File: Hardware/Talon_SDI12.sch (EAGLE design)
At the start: 100 parts, among them J1 CONN_APOGEE_LOGGER, J2 CONN_TALON_REMOTE, J3 CONN_SDI-12_LOGGERM8_TE_BOARD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, J4 CONN_SDI-12_LOGGERM8_TE_BOARD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, J5 CONN_SDI-12_LOGGERM8_TE_BOARD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, Q1 2N7002, Q2 2N7002, Q3 2N7002, Q4 2N7002, Q5 AO3419, Q6 AO3419, Q7 AO3419, Q8 AO3419, U1 SN74HC04, U10 FXMAR2102UMLP, U11 74HC4852, U12 SN74AUP1T157DCK, U13 MCP3221, U14 MCP23018QFN, U15 PCA9536DFN, U16 MCP3421A3, U17 SN74LVC1G3157SC70, U18 SN74LVC1G3157SC70, U19 SN74LVC1G3157SC70, U2 CD4044, U20 SN74LVC1G3157SC70, U21 SN74LVC1G00SC70, U22 SN74LVC2G241DCU, U23 SN74LVC1G17DCK, U24 24AA02SOT23, U3 SIP32431TDFN, U4 INA4180A2, U5 MAX9034TSSOP, U6 SI1869, U7 SN74AC08, U8 LM2621, U9 LMR62014SOT23

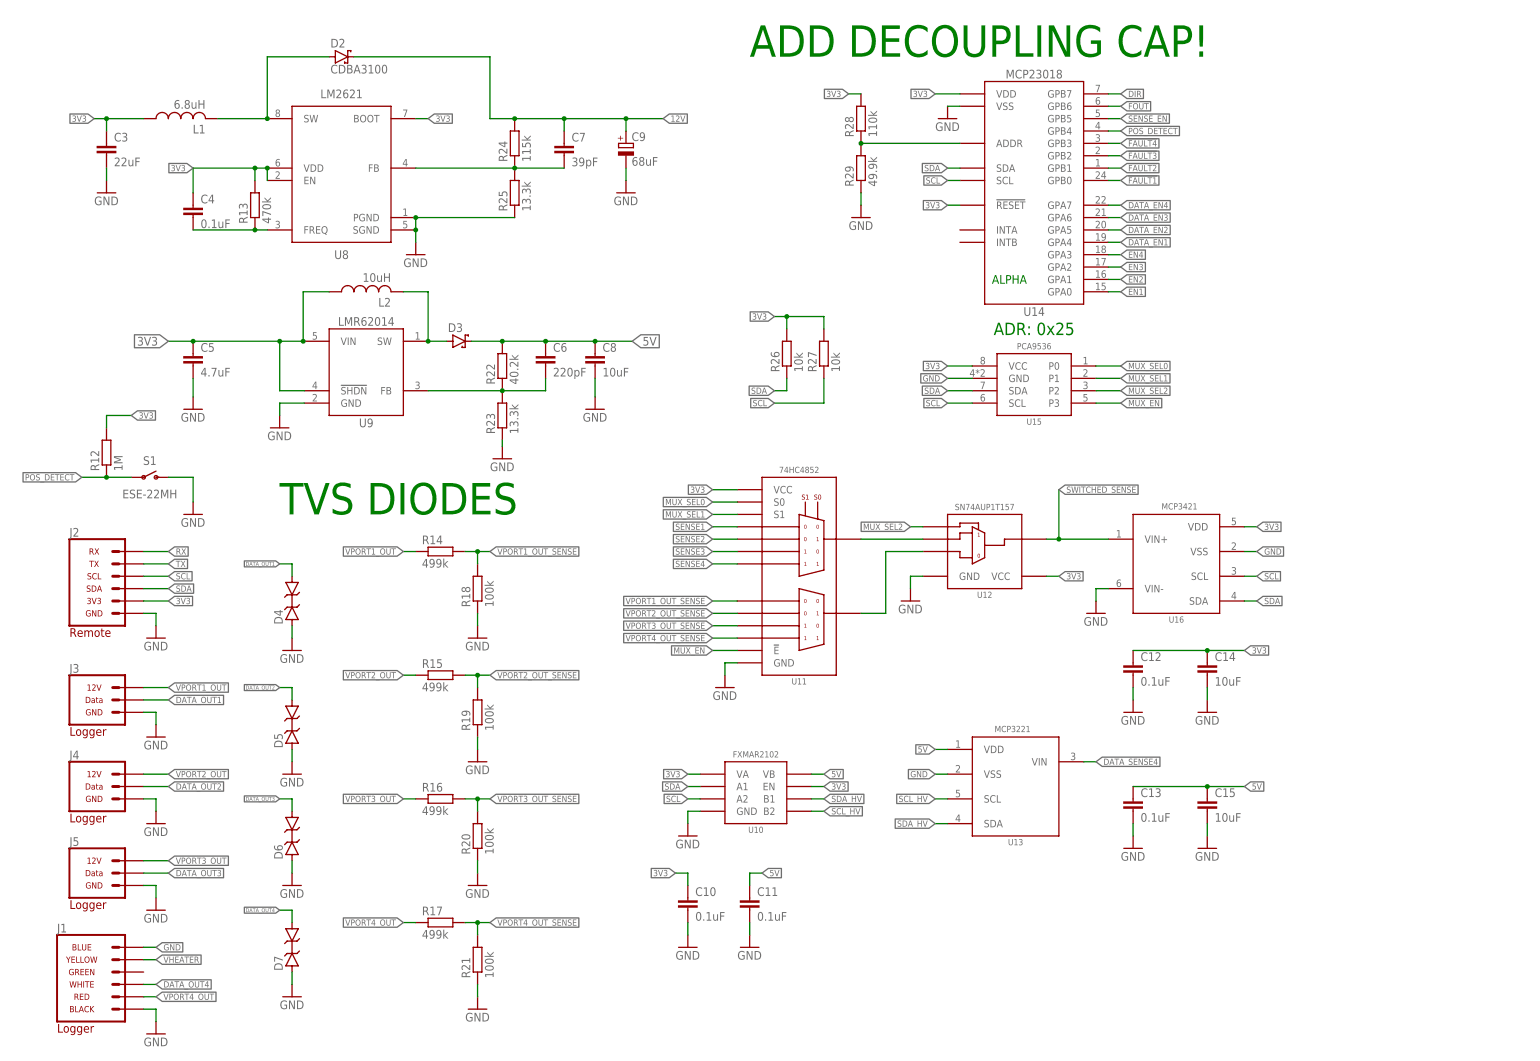
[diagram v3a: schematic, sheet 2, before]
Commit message: Updated v1.0, sent to fab
Made fixes for v1.0:
- Fixed bypass control
- Changed arrangement of 12V reg
- Added filter lines (clitch protection) to sense lines
- Flipped Talon connector port pinout
- Adjusted port 4 topology to deal with pulldown issue
- Moved MUX (U11/U15) to prevent soldering issues 
- Moved U7 to prevent bumping 
- Added additional protection circuitry on SDI-12 outputs
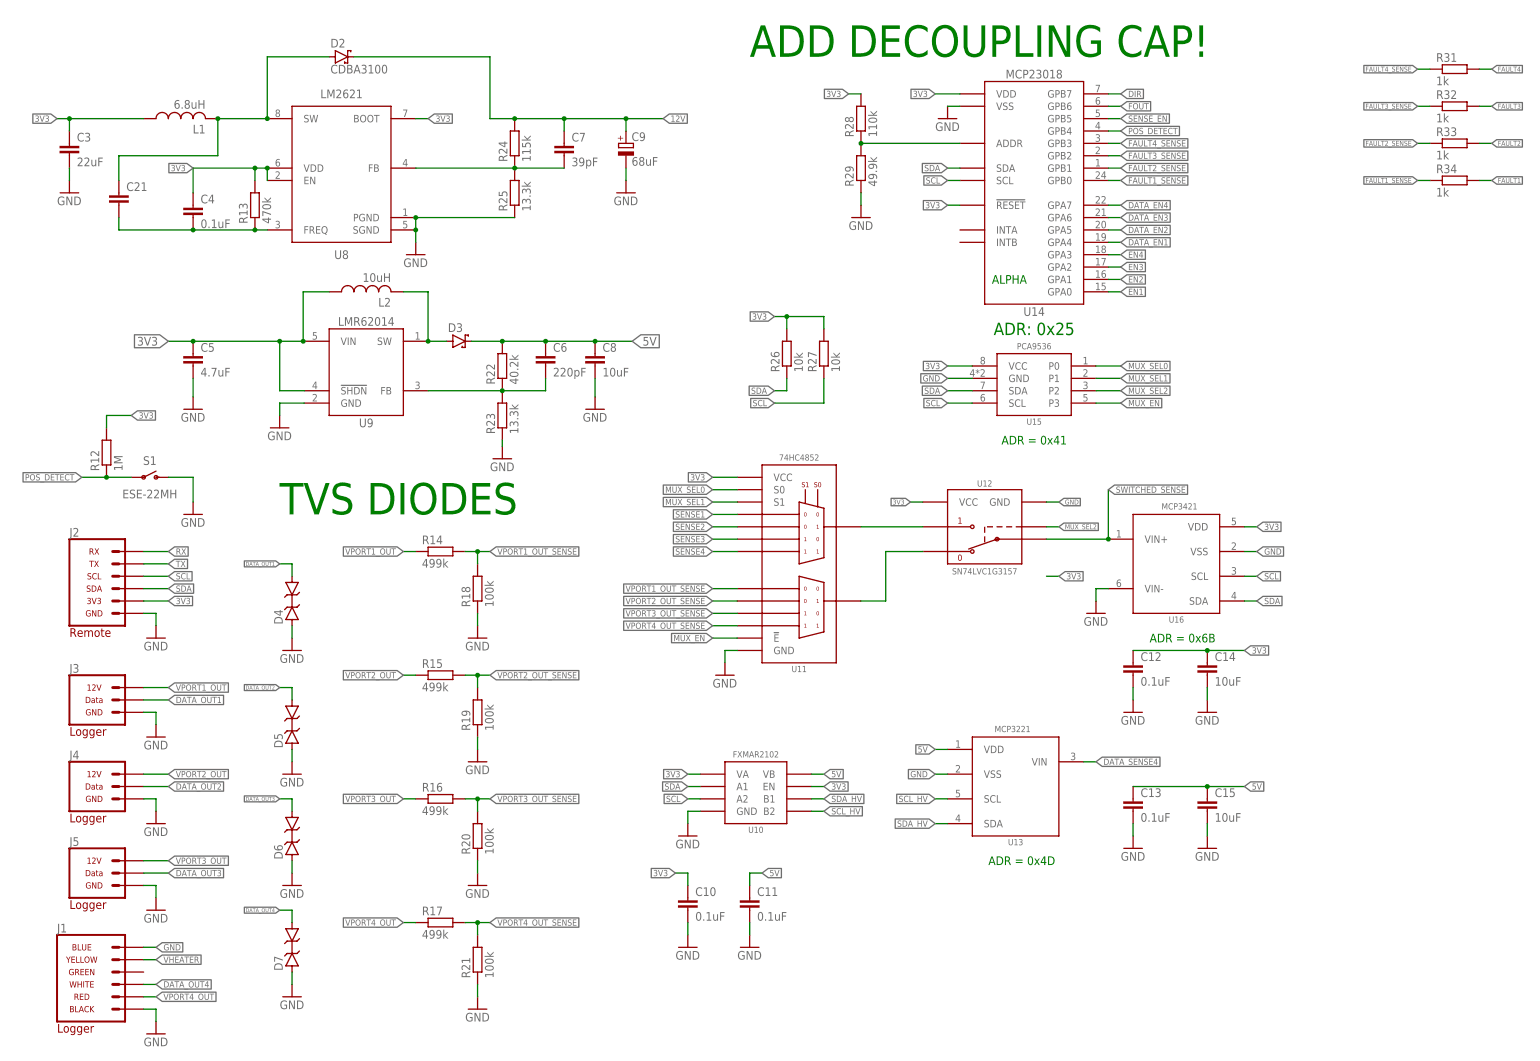
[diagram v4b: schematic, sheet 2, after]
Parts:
- removed R30: 100k, bschulz_passives:R-EU_100KR0402
- added C17, C18, C19, C20: 0.1uF, bschulz_passives:C-EU0.1UFC0402
- added C21: (no value), bschulz_passives:C-EUC0402
- added C22: 3.3nF, bschulz_passives:C-EUC0402
- added D10, D11, D8, D9: (no value), bschulz:DIODE_ZENERSOD-323
- added R31, R32, R33, R34, R35, R36, R37, R38: 1k, bschulz_passives:R-EU_1KR0402
- added R39: 200K, bschulz_passives:R-EU_200KR0402
- added R40, R41, R42, R43, R44: 510R, bschulz_passives:R-EU_R0402
- U12: value SN74AUP1T157DCK -> SN74LVC1G3157SC70; device bschulz:SN74AUP1T157DCK -> bschulz:SN74LVC1G3157SC70
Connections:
- new net !DATA_EN4: U1.Y5, U20.S, U6.EN
- new net DATA_OUT_PROTEC1: D8.C, R40.2, U17.A
- new net DATA_OUT_PROTEC2: D9.C, R42.2, U18.A
- new net DATA_OUT_PROTEC3: D10.C, R43.2, U19.A
- new net DATA_OUT_PROTEC4: D11.C, R44.2, U20.A
- new net DATA_PROTEC: R41.2, U22.1A, U22.2Y
- new net FAULT1_SENSE: R34.1, U14.GPB0
- new net FAULT2_SENSE: R33.1, U14.GPB1
- new net FAULT3_SENSE: R32.1, U14.GPB2
- new net FAULT4_SENSE: R31.1, U14.GPB3
- new net SENSE1_FILT: C17.1, R35.2, U5.INA-
- new net SENSE2_FILT: C18.1, R36.2, U5.INB-
- new net SENSE3_FILT: C19.1, R37.2, U5.INC-
- new net SENSE4_FILT: C20.1, R38.2, U5.IND-
- net !FAULT1: now also U1.Y4, U7.B4; no longer U1.A4, U14.GPB0, U2.Q2
- net !FAULT2: now also U1.Y2, U7.B1; no longer U1.A2, U14.GPB1, U2.Q1
- net !FAULT3: now also U1.Y3, U7.B3; no longer U1.A3, U14.GPB2, U2.Q3
- net !FAULT4: now also U1.Y1, U7.B2; no longer U1.A1, U14.GPB3, U2.Q4
- net 3V3: no longer U1.A5, U2.EN
- net DATA: now also C22.1, R39.2, R41.1, U20.B1; no longer U20.B2, U22.1A, U22.2Y
- net DATA_EN4: now also U1.A5; no longer R30.2, U20.S, U6.EN
- net DATA_OUT1: now also R40.1; no longer U17.A
- net DATA_OUT2: now also R42.1; no longer U18.A
- net DATA_OUT3: now also R43.1; no longer U19.A
- net DATA_OUT4: now also R44.1; no longer U20.A
- net DATA_SENSE4: now also U20.B2; no longer U20.B1
- net FAULT1: now also R34.2, U1.A4, U2.Q2; no longer U1.Y4, U7.B4
- net FAULT2: now also R33.2, U1.A2, U2.Q1; no longer U1.Y2, U7.B1
- net FAULT3: now also R32.2, U1.A3, U2.Q3; no longer U1.Y3, U7.B3
- net FAULT4: now also R31.2, U1.A1, U2.Q4; no longer U1.Y1, U7.B2
- net GND: now also C17.2, C18.2, C19.2, C20.2, C22.2, D10.A, D11.A, D8.A, D9.A, R39.1; no longer R30.1
- net MUX_SEL2: now also U12.S; no longer U12.C
- net N$18: now also U12.B1; no longer U12.B
- net N$38: now also U12.B2; no longer U12.A
- net N$7: now also C21.2
- net N$8: now also C21.1
- net SENSE1: now also R35.1; no longer U5.INA-
- net SENSE2: now also R36.1; no longer U5.INB-
- net SENSE3: now also R37.1; no longer U5.INC-
- net SENSE4: now also R38.1; no longer U5.IND-
- net SENSE_EN: now also U2.EN
- net SWITCHED_SENSE: now also U12.A; no longer U12.Y
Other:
- note added: "ADR = 0x41"
- note added: "ADR = 0x4D"
- note added: "ADR = 0x6B"
- moved on the sheet: C3, U11, U21, U24

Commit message: v1.3 Updates
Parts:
- R18, R19, R20, R21: device bschulz_passives:R-EU_100KR0603 -> bschulz_passives:R-EU_100KR0402
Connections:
- net !DATA_EN4: no longer U6.EN
- net DATA_EN4: now also U6.EN
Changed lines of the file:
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@@
 <part name="FRAME2" library="bschulz" deviceset="FRAME_A_L" device=""/>
 <part name="R14" library="bschulz_passives" deviceset="R-EU_" device="R0603" technology="499K" value="499k"/>
-<part name="R18" library="bschulz_passives" deviceset="R-EU_" device="R0603" technology="100K" value="100k"/>
+<part name="R18" library="bschulz_passives" deviceset="R-EU_" device="R0402" technology="100K" value="100k"/>
 <part name="R15" library="bschulz_passives" deviceset="R-EU_" device="R0603" technology="499K" value="499k"/>
-<part name="R19" library="bschulz_passives" deviceset="R-EU_" device="R0603" technology="100K" value="100k"/>
+<part name="R19" library="bschulz_passives" deviceset="R-EU_" device="R0402" technology="100K" value="100k"/>
 <part name="R16" library="bschulz_passives" deviceset="R-EU_" device="R0603" technology="499K" value="499k"/>
-<part name="R20" library="bschulz_passives" deviceset="R-EU_" device="R0603" technology="100K" value="100k"/>
+<part name="R20" library="bschulz_passives" deviceset="R-EU_" device="R0402" technology="100K" value="100k"/>
 <part name="R17" library="bschulz_passives" deviceset="R-EU_" device="R0603" technology="499K" value="499k"/>
-<part name="R21" library="bschulz_passives" deviceset="R-EU_" device="R0603" technology="100K" value="100k"/>
+<part name="R21" library="bschulz_passives" deviceset="R-EU_" device="R0402" technology="100K" value="100k"/>
 <part name="GND29" library="supply1" library_urn="urn:adsk.eagle:library:371" deviceset="GND" device=""/>
 <part name="GND30" library="supply1" library_urn="urn:adsk.eagle:library:371" deviceset="GND" device=""/>
@@
 <label x="106.68" y="172.72" size="0.8128" layer="95" rot="R180" xref="yes"/>
 </segment>
+<segment>
+<pinref part="U6" gate="G$1" pin="EN"/>
+<wire x1="215.9" y1="66.04" x2="210.82" y2="66.04" width="0.1524" layer="91"/>
+<label x="210.82" y="66.04" size="0.8128" layer="95" rot="R180" xref="yes"/>
+</segment>
 </net>
 <net name="!DATA_EN4" class="0">
@@
 <label x="132.08" y="172.72" size="0.8128" layer="95" xref="yes"/>
 </segment>
-<segment>
-<pinref part="U6" gate="G$1" pin="EN"/>
-<wire x1="215.9" y1="66.04" x2="210.82" y2="66.04" width="0.1524" layer="91"/>
-<label x="210.82" y="66.04" size="0.8128" layer="95" rot="R180" xref="yes"/>
-</segment>
-</net>
+</net>

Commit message: Updates for BoM
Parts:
- C17, C18, C19, C20, C4: value 0.1uF -> DNP; DIGIKEY (none) -> DNP; MF (none) -> N/A; MPN (none) -> DNP
- C21: value (none) -> 1pF; device bschulz_passives:C-EUC0402 -> bschulz_passives:C-EU1PFC0402
- C22: device bschulz_passives:C-EUC0402 -> bschulz_passives:C-EU3.3NFC0402
- C9: value 68uF -> 100uF; DIGIKEY 399-3803-1-ND -> 718-293D107X0016D2TE3CT-ND; MF Kemet -> Vishay; MPN T491D686K020AT -> 293D107X0016D2TE3
- D10, D11, D8, D9: value (none) -> 5.1V; DIGIKEY (none) -> BZX384B5V1-HE3-08GICT-ND; MF (none) -> Vishay; MPN (none) -> BZX384B5V1-HE3-08
- D4, D5, D6, D7: value 6V -> 12V; DIGIKEY (none) -> D12V0L1B2LP-7BDICT-ND; MPN (none) -> D12V0L1B2LP-7B
- R13: value 470k -> 390k; device bschulz_passives:R-EU_470KR0603 -> bschulz_passives:R-EU_390KR0603
- R40, R41, R42, R43, R44: device bschulz_passives:R-EU_R0402 -> bschulz_passives:R-EU_510R0402
- U23: DIGIKEY (none) -> 296-11608-1-ND; DISP (none) -> SN74LVC1G14; MPN (none) -> SN74LVC1G14DCKR
- U8: DIGIKEY (none) -> LM2623AMM/NOPBCT-ND; DISP (none) -> LM2623; MPN (none) -> LM2623AMM/NOPB
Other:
- note removed: "REPLACE! SN74LVC1G14"
